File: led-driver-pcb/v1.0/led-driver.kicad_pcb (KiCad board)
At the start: 2 copper layers, 66 x 50 mm, 33 parts, among them P1 POWER, P2 CTRL, P3 LED, Q1 MOSFET_N, Q2 MOSFET_N, U1 MAX16834

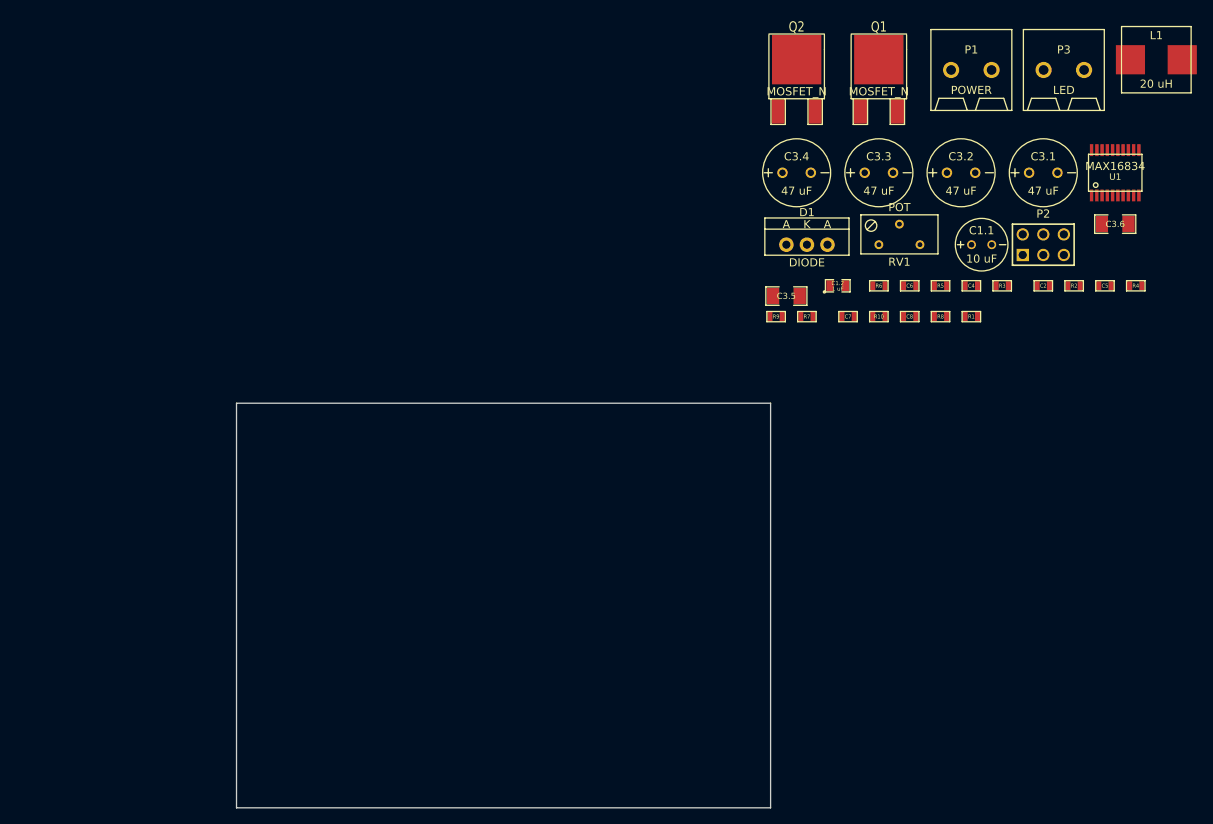
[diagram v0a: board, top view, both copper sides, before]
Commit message: arranged components on PCB
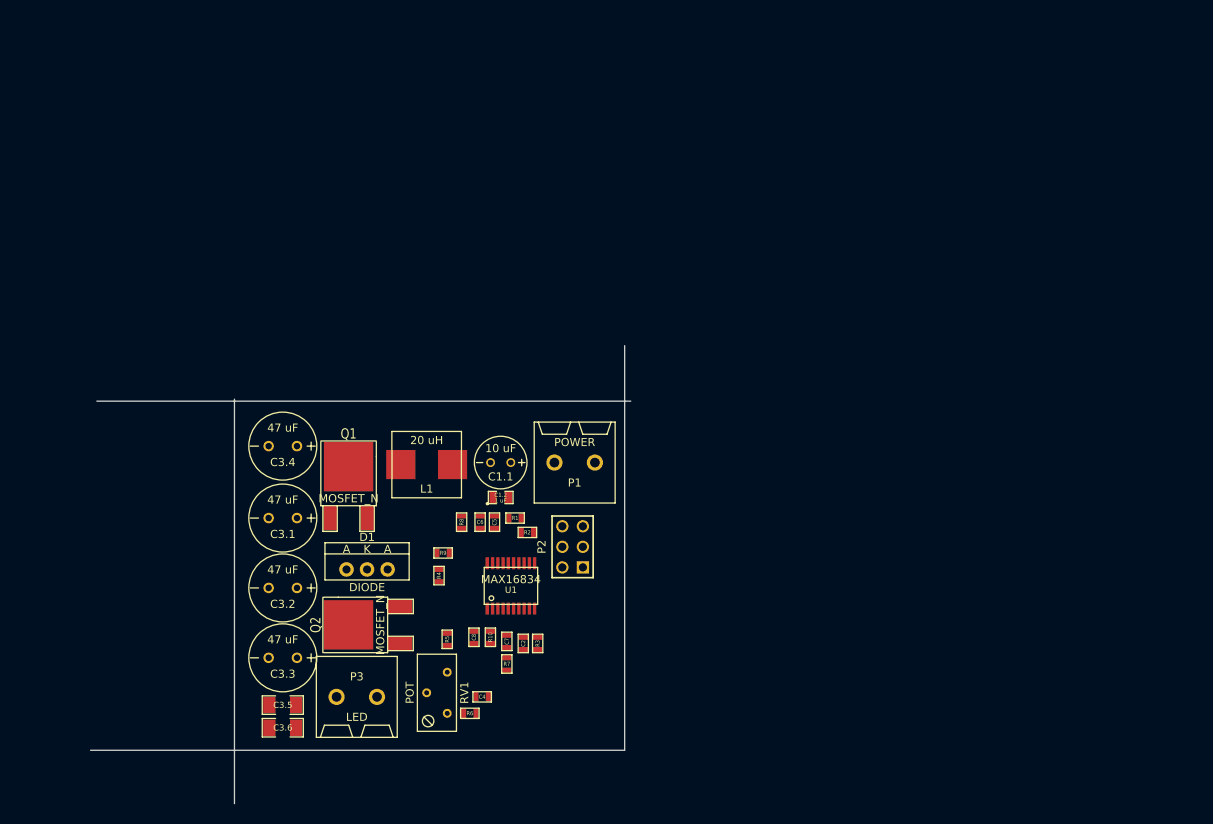
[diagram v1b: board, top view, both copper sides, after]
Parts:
- moved C3.6 120.2 mm to (172.7, 165.1)
- moved P3 116.8 mm to (181.9, 161.3)
- moved C3.1 103.2 mm to (172.7, 139.2), turned to 180 degrees
- moved L1 103.1 mm to (190.5, 132.6), turned to 180 degrees
- moved C3.2 98.3 mm to (172.7, 147.8), turned to 180 degrees
- moved C3.3 95.0 mm to (172.7, 156.5), turned to 180 degrees
- moved R4 93.3 mm to (192.0, 146.3), turned to 90 degrees
- moved U1 90.5 mm to (200.9, 147.6)
- moved Q1 82.6 mm to (180.8, 139.2)
- moved C5 80.9 mm to (198.9, 139.7), turned to 90 degrees
- moved Q2 80.2 mm to (187.2, 152.4), turned to 90 degrees
- moved C3.5 80.2 mm to (172.7, 162.3)
- moved C4 79.0 mm to (197.4, 161.3), turned to 180 degrees
- moved RV1 78.7 mm to (193.0, 160.8), turned to 90 degrees
- moved C2 78.0 mm to (202.4, 154.7), turned to 90 degrees
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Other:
- board size 66 x 50 mm -> 66.8 x 56.6 mm

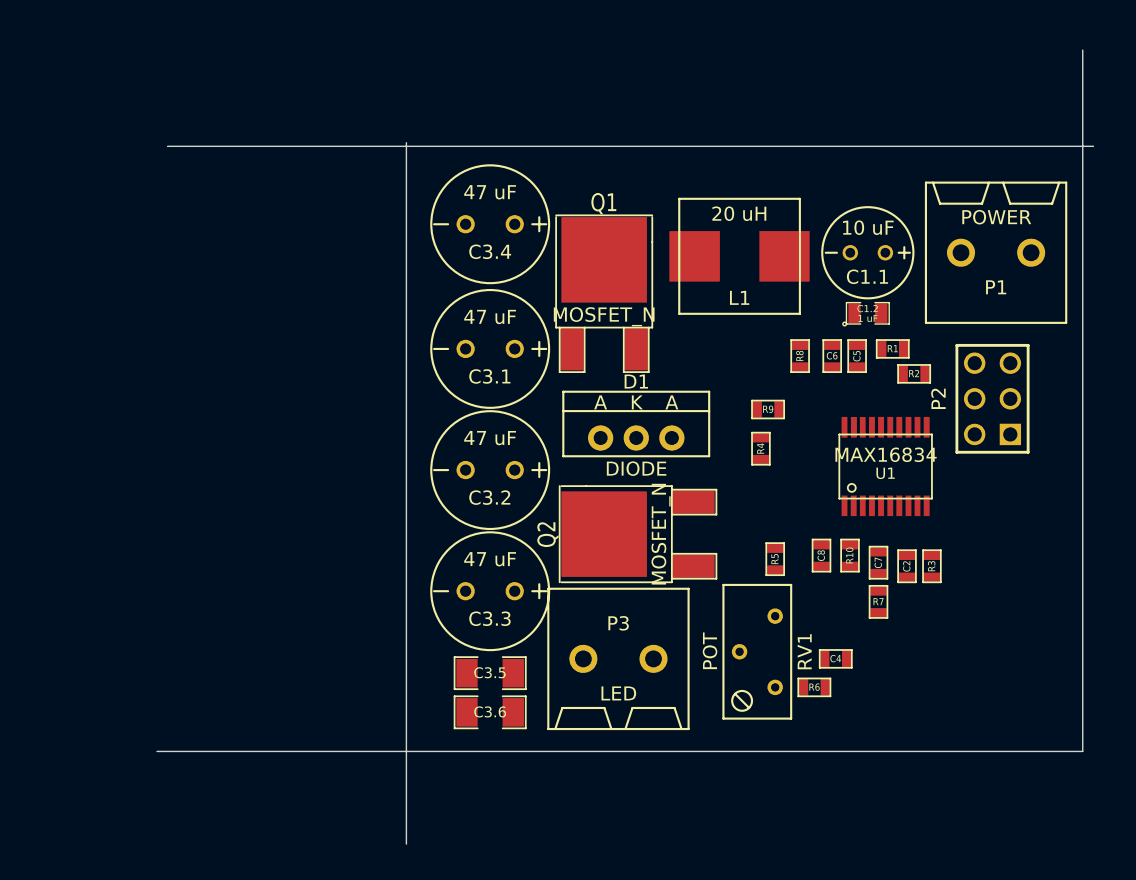
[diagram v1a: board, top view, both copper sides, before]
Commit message: updated components on PCB
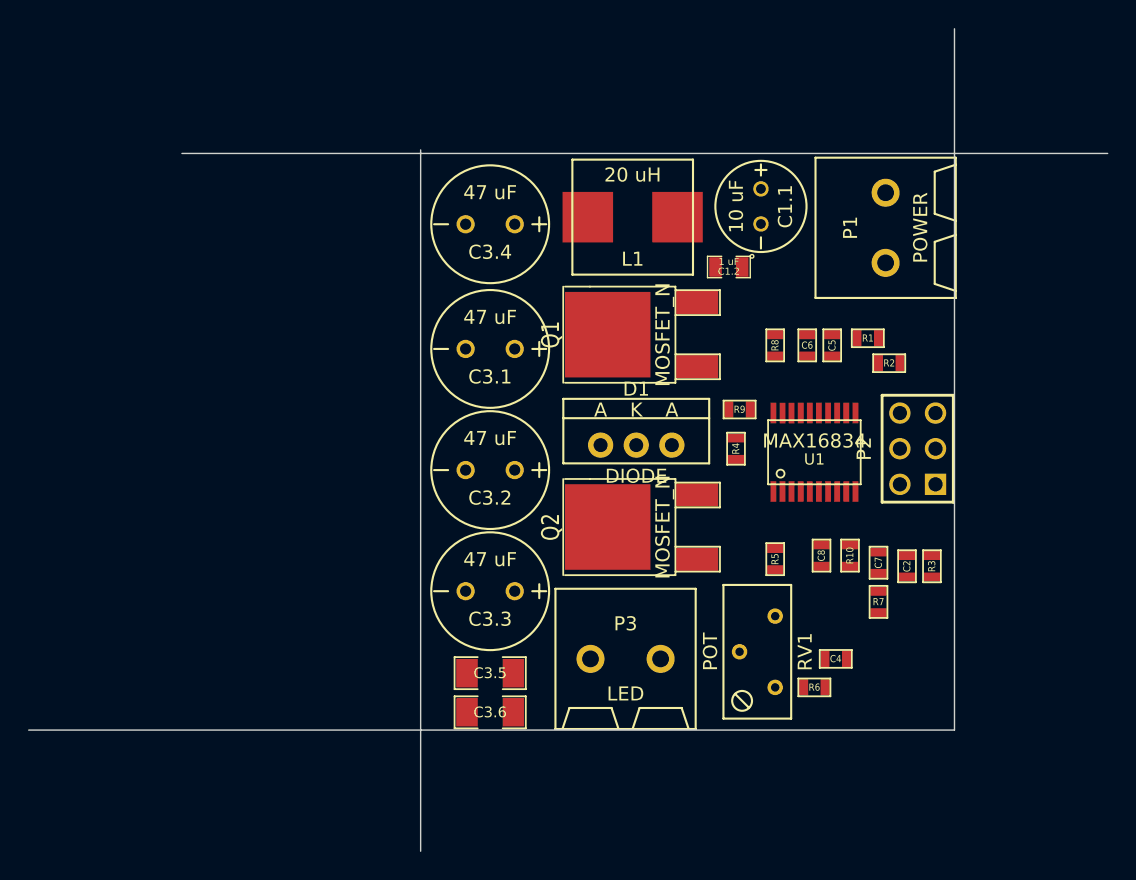
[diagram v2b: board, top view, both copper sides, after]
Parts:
- moved C1.2 10.4 mm to (189.7, 133.3), turned to 180 degrees
- moved C1.1 8.30 mm to (192.0, 129.0), turned to 270 degrees
- moved L1 8.12 mm to (182.9, 129.8)
- moved P1 8.07 mm to (200.9, 130.6), turned to 90 degrees
- moved Q1 6.68 mm to (187.5, 138.2), turned to 90 degrees
- moved P2 6.41 mm to (203.2, 146.3)
- moved U1 5.18 mm to (195.8, 146.6)
- moved R9 2.03 mm to (190.5, 143.5)
- moved C6 1.93 mm to (195.3, 138.9)
- moved R8 1.93 mm to (193.0, 138.9)
- moved C5 1.93 mm to (197.1, 138.9)
- moved R1 1.93 mm to (199.6, 138.4)
- moved R2 1.93 mm to (201.2, 140.2)
- moved R4 1.78 mm to (190.2, 146.3)
- moved Q2 0.57 mm to (187.5, 151.9)
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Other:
- board size 66.8 x 56.6 mm -> 76.9 x 58.6 mm

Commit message: updated layout, added screwholes
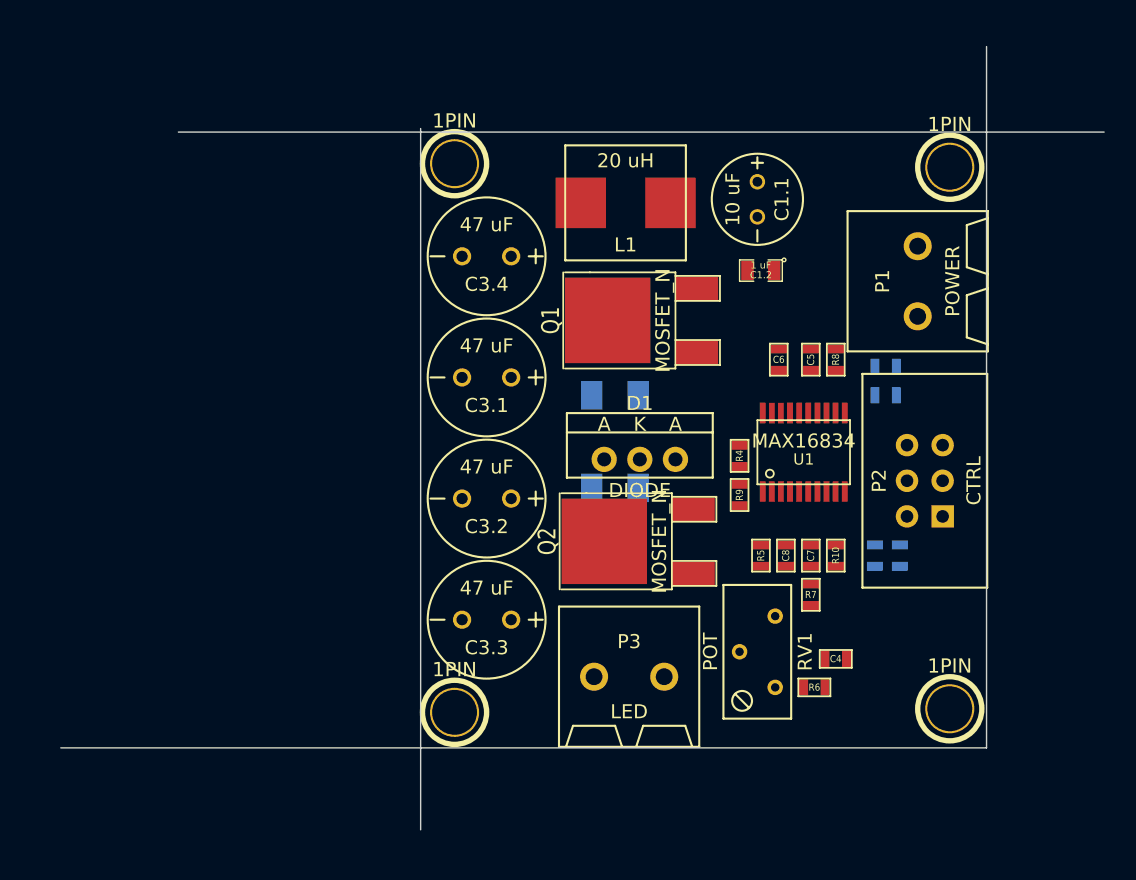
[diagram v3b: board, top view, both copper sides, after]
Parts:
- added 1PIN: P***, 1pin, F.Cu at (170.2, 126.0)
- added 1PIN: P***, 1pin, F.Cu at (205.5, 126.2)
- added 1PIN: P***, 1pin, F.Cu at (205.5, 164.8)
- added 1PIN: P***, 1pin, F.Cu at (170.2, 165.1)
- C2, C3.5, C3.6, R1, R2, R3: moved to B.Cu
- P2: footprint pin_array_3x2 -> PinHeader3x2
- moved C3.6 24.3 mm to (181.6, 142.5)
- moved C3.5 15.9 mm to (181.6, 149.1)
- moved R9 6.10 mm to (190.5, 149.6), turned to 270 degrees
- moved R7 4.85 mm to (195.6, 156.7)
- moved C7 4.85 mm to (195.6, 153.9)
- moved P1 4.44 mm to (203.2, 134.4)
- moved R8 4.44 mm to (197.4, 140.0)
- moved C8 2.54 mm to (193.8, 153.9)
- moved C2 2.41 mm to (200.2, 153.9), turned to 270 degrees
- moved R3 2.41 mm to (201.9, 153.9), turned to 90 degrees
- moved R1 2.40 mm to (200.9, 140.5), turned to 180 degrees
- moved P2 2.34 mm to (203.7, 148.6)
- moved C1.2 2.30 mm to (192.0, 133.6)
- moved R2 2.30 mm to (200.9, 142.5)
- moved C3.4 2.30 mm to (172.5, 132.6)
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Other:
- board size 76.9 x 58.6 mm -> 74.4 x 55.8 mm

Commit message: Finished the PCB design.
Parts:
- removed 1PIN (x4): P***, 1pin
- added M3A: P***, 1pin, F.Cu at (213.0, 129.0)
- added M3B: P***, 1pin, F.Cu at (182.0, 129.0)
- added M3C: P***, 1pin, F.Cu at (182.0, 171.0)
- added M3D: P***, 1pin, F.Cu at (213.0, 171.0)
- C1.2, D1, R5, R6: moved to B.Cu
- C2, C3.5, C3.6, R3: moved to F.Cu
- C8: footprint SM0603 -> SM0805; moved to B.Cu
- R10, R8: footprint SM0603 -> SM2512; moved to B.Cu
- moved RV1 26.5 mm to (214.2, 144.9)
- moved R2 25.3 mm to (201.0, 167.8), turned to 270 degrees
- moved R1 24.5 mm to (201.0, 165.0), turned to 270 degrees
- moved R5 22.8 mm to (211.7, 142.4)
- moved R6 22.4 mm to (211.7, 147.5), turned to 90 degrees
- moved C1.1 22.3 mm to (212.7, 136.3)
- moved P2 17.7 mm to (205.1, 166.3), turned to 270 degrees
- moved C3.5 16.4 mm to (198.0, 150.0), turned to 90 degrees
- moved C3.6 15.3 mm to (194.9, 150.0), turned to 90 degrees
- moved C1.2 12.8 mm to (204.1, 129.2)
- moved Q2 12.4 mm to (198.0, 159.1)
- moved P3 12.0 mm to (192.9, 168.8)
- moved C3.3 12.0 mm to (183.2, 163.7)
- moved C4 11.9 mm to (206.3, 153.6), turned to 90 degrees
- moved C3.2 11.8 mm to (183.2, 154.6)
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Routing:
- net N-0000010: track 0.00 -> 181.6 mm, vias 0 -> 3
- net N-0000011: track 0.00 -> 53.4 mm
- net N-000008: track 0.00 -> 40.2 mm
- net N-000005: track 0.00 -> 36.8 mm
- net N-0000022: track 0.00 -> 25.0 mm, vias 0 -> 1
- net N-0000023: track 0.00 -> 22.3 mm, vias 0 -> 1
- net N-0000015: track 0.00 -> 21.5 mm, vias 0 -> 4
- net GND: track 0.00 -> 21.4 mm, vias 0 -> 9
- net N-0000021: track 0.00 -> 17.3 mm
- net N-000004: track 0.00 -> 17.2 mm
- net N-000001: track 0.00 -> 16.3 mm
- net N-0000013: track 0.00 -> 13.9 mm
- net N-0000012: track 0.00 -> 11.2 mm
- net N-000006: track 0.00 -> 9.97 mm, vias 0 -> 1
- net N-000002: track 0.00 -> 9.01 mm
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- added copper zone on B.Cu, net GND
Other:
- board size 74.4 x 55.8 mm -> 37 x 48 mm
- net class Default: clearance 0.254 -> 0.15; trace_width 0.254 -> 0.4; via_dia 0.889 -> 0.6; via_drill 0.635 -> 0.3
- rule trace_clearance: 0.254 -> 0.15
- rule trace_min: 0.254 -> 0.15
- rule via_min_drill: 0.508 -> 0.3
- rule via_min_size: 0.889 -> 0.6
- board text added: "LED Driver v0.1 P. Eller + M. Rossini"

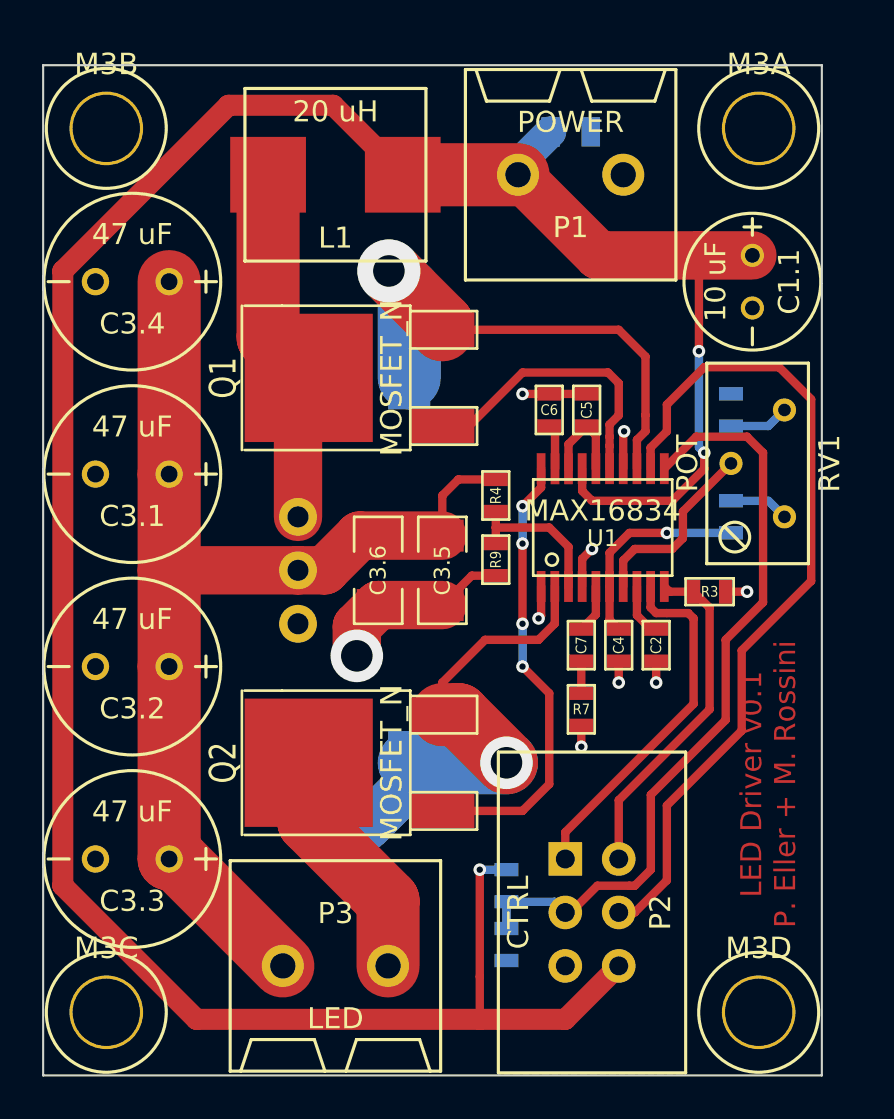
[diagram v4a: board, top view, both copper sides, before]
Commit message: added pwrgnd layer
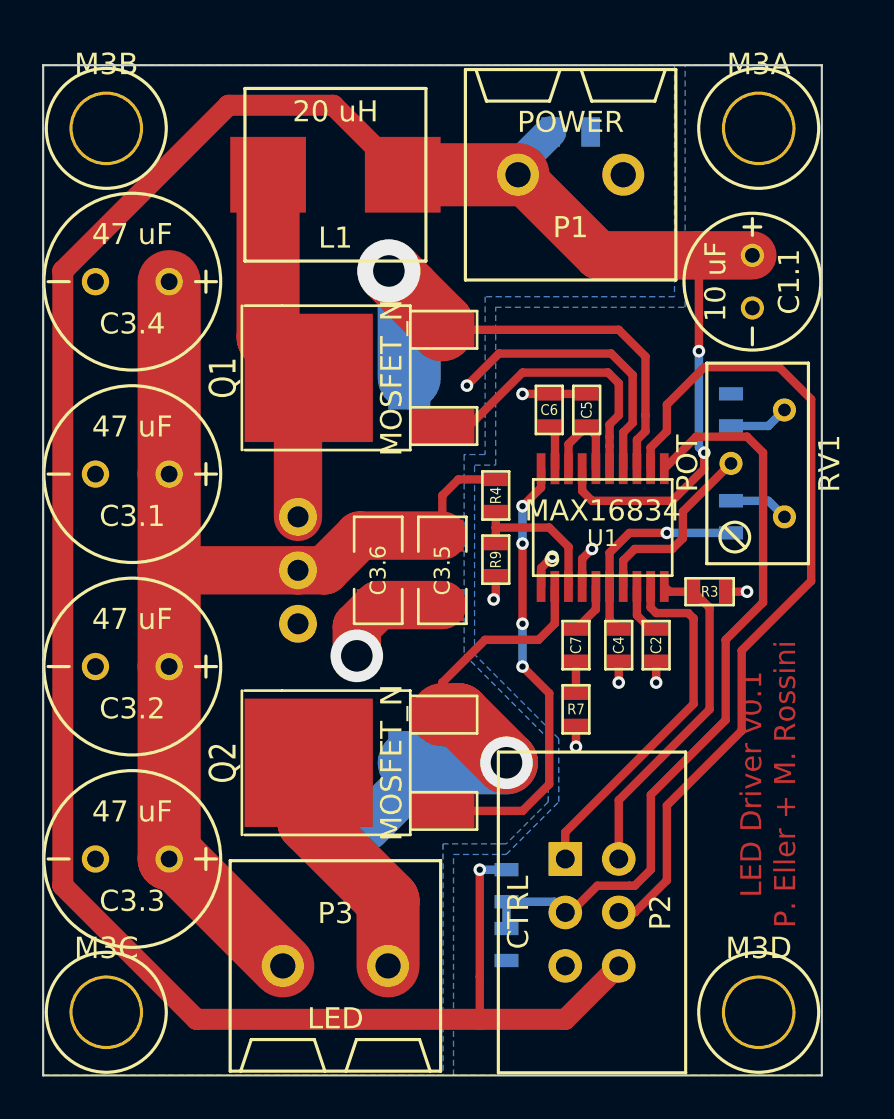
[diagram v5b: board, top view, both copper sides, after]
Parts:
- added RGND0: 0, SM0603, B.Cu at (209.2, 135.0)
- moved C7 0.25 mm to (204.3, 153.6)
- moved R7 0.25 mm to (204.3, 156.6)
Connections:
- C1.2 pad 1: GND -> GNDPWR
- C3.1 pad 2: GND -> GNDPWR
- C3.2 pad 2: GND -> GNDPWR
- C3.3 pad 2: GND -> GNDPWR
- C3.4 pad 2: GND -> GNDPWR
- C3.5 pad 1: GND -> GNDPWR
- C3.6 pad 1: GND -> GNDPWR
- C8 pad 1: GND -> GNDPWR
- P1 pad 1: GND -> GNDPWR
- R10 pad 2: GND -> GNDPWR
- R8 pad 2: GND -> GNDPWR
- U1 pad 14: GND -> GNDPWR
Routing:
- net GNDPWR: track 0.00 -> 19.4 mm, vias 0 -> 2
- net GND: track 21.4 -> 11.9 mm, vias 9 -> 8
- added copper zone on B.Cu, net GNDPWR

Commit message: Optimized design and put capacitor C1.1 also to power ground.
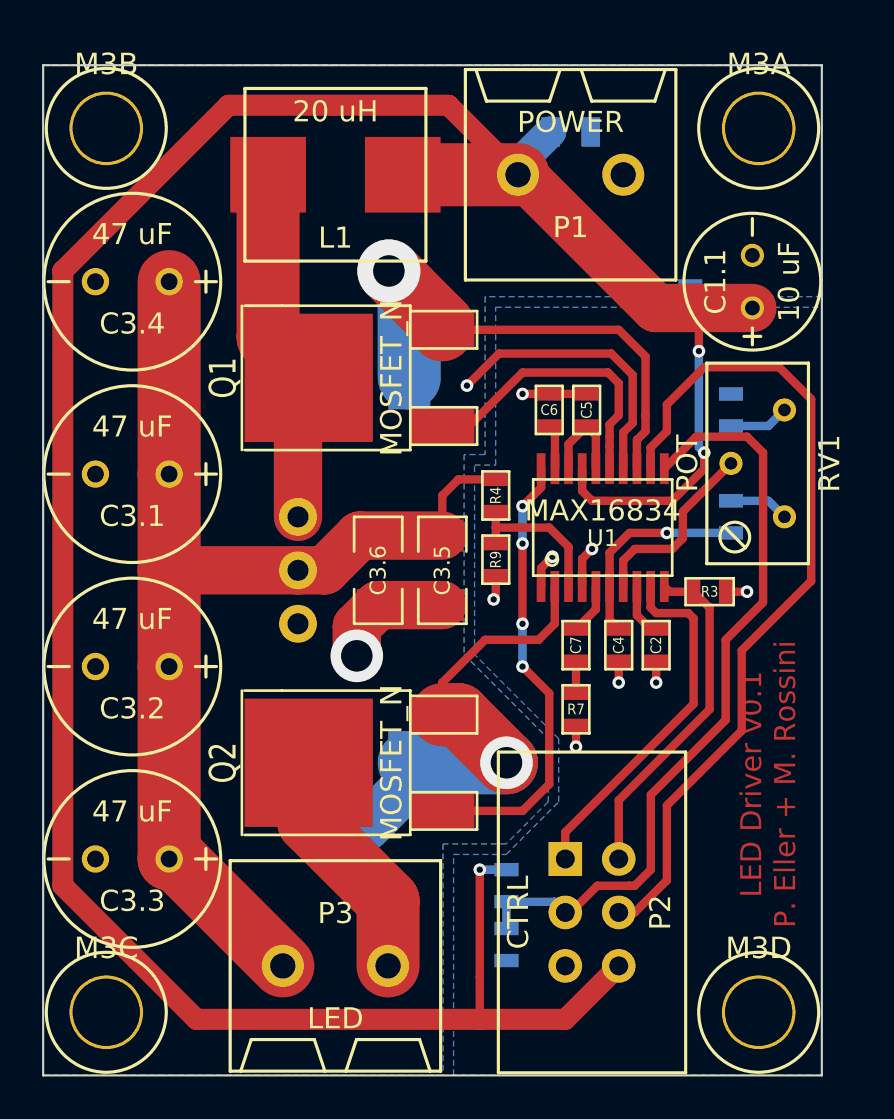
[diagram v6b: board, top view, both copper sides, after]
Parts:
- moved RGND0 2.30 mm to (209.8, 137.2), turned to 270 degrees
- turned C1.1 to 90 degrees
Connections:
- C1.1 pad 2: GND -> GNDPWR
- RGND0 pad 1: GND -> (no net)
- RGND0 pad 2: GNDPWR -> GND
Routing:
- net N-0000010: track 181.6 -> 185.6 mm

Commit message: Made more optimizations.
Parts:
- moved C5 0.25 mm to (204.6, 142.4)
- moved C6 0.25 mm to (202.8, 142.4)
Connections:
- C5 pad 2: GND -> GNDPWR
- RGND0 pad 1: (no net) -> GNDPWR
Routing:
- net GNDPWR: track 19.4 -> 27.4 mm, vias 2 -> 3
- net GND: track 11.9 -> 10.1 mm
- net N-000003: track 9.01 -> 9.60 mm
- net N-0000010: track 4.60 -> 4.09 mm
